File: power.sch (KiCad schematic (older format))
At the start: 32 parts, among them J2 4DB-P108-06, J3 39531-1002, J4 39531-1002, U2 AP1501A-50K5G-13, U3 AP2112K-3.3TRG1

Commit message: Current snapshot
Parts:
- added FB1: MPZ1608S221A, Resistor_SMD:R_0603_1608Metric, symbol Device:Ferrite_Bead_Small
- added JP2: Jumper_3_Bridged12, Connector_PinHeader_2.54mm:PinHeader_1x03_P2.54mm_Vertical, symbol Jumper:Jumper_3_Bridged12
- C1, C3, C4, C5, C6: footprint Capacitor_SMD:CP_Elec_6.3x7.7 -> Capacitor_SMD:CP_Elec_6.3x5.7
- C14: value 10uF -> 22uF; footprint Capacitor_SMD:C_0603_1608Metric -> Capacitor_SMD:C_1206_3216Metric
- C15: footprint Capacitor_SMD:C_0603_1608Metric -> Capacitor_SMD:C_1206_3216Metric
- J2: Note (none) -> Alternative: OSTYK42106030
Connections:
- net VDD24V: now also JP2.3 (B)
- net VDD5V: now also FB1.2, JP2.1 (A); no longer C14.1, U3.1 (IN), U3.3 (EN)
- new net: C14.1, FB1.1, U3.1 (IN), U3.3 (EN)
- new net VDD_FAN: JP2.2 (C)
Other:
- note added: "FAN Voltage Selection"
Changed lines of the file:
@@
 $Descr A4 11693 8268
 encoding utf-8
-Sheet 3 7
+Sheet 3 11
 Title ""
 Date ""
@@
 F 0 "C1" H 1368 1946 50  0000 L CNN
 F 1 "100uF" H 1368 1855 50  0000 L CNN
-F 2 "Capacitor_SMD:CP_Elec_6.3x7.7" H 1288 1750 50  0001 C CNN
-F 3 "https://www.mouser.de/ProductDetail/Wurth-Electronics/865080545012?qs=0KOYDY2FL297tvB6LOdg5A%3d%3d" H 1250 1900 50  0001 C CNN
+F 2 "Capacitor_SMD:CP_Elec_6.3x5.7" H 1288 1750 50  0001 C CNN
+F 3 "" H 1250 1900 50  0001 C CNN
 	1    1250 1900
 	1    0    0    -1
@@
 Wire Wire Line
 	2750 1000 5050 1000
-$Comp
-L Device:C C14
-U 1 1 5BC5B3FE
-P 7000 1900
-F 0 "C14" H 7115 1946 50  0000 L CNN
-F 1 "10uF" H 7115 1855 50  0000 L CNN
-F 2 "Capacitor_SMD:C_0603_1608Metric" H 7038 1750 50  0001 C CNN
-F 3 "~" H 7000 1900 50  0001 C CNN
-	1    7000 1900
-	1    0    0    -1
-$EndComp
-$Comp
-L Device:C C15
-U 1 1 5BC5B47D
-P 8450 1900
-F 0 "C15" H 8565 1946 50  0000 L CNN
-F 1 "10uF" H 8565 1855 50  0000 L CNN
-F 2 "Capacitor_SMD:C_0603_1608Metric" H 8488 1750 50  0001 C CNN
-F 3 "~" H 8450 1900 50  0001 C CNN
-	1    8450 1900
-	1    0    0    -1
-$EndComp
 $Comp
 L Device:R R6
@@
 Wire Wire Line
 	9100 1750 8900 1750
-Connection ~ 8450 1750
-Wire Wire Line
-	8450 1750 8250 1750
 Connection ~ 8900 1750
 Wire Wire Line
-	8900 1750 8450 1750
-Wire Wire Line
-	7000 1750 7350 1750
-Wire Wire Line
 	7350 1750 7350 2050
 Wire Wire Line
 	7350 2050 7550 2050
-Connection ~ 7350 1750
 Wire Wire Line
 	7350 1750 7550 1750
@@
 	1    0    0    -1
 $EndComp
-Text GLabel 6700 1750 0    50   Input ~ 0
+Text GLabel 6350 1750 0    50   Input ~ 0
 VDD5V
-Wire Wire Line
-	6700 1750 7000 1750
-Connection ~ 7000 1750
 Text Notes 1850 800  0    157  ~ 31
 5V Power supply
@@
 F 2 "heteromycin:4DB-P108-06" H 1200 4000 50  0001 C CNN
 F 3 "https://www.mouser.de/datasheet/2/418/NG_CD_2-1437667-4_N8-639207.pdf" H 1200 4000 50  0001 C CNN
+F 4 "Alternative: OSTYK42106030" H 1200 4000 50  0001 C CNN "Note"
 	1    1200 4000
 	-1   0    0    -1
@@
 Text GLabel 4150 3800 2    50   Input ~ 0
 VDD24V
-Text HLabel 4200 4400 2    50   Input ~ 0
-VDD_HEAT1
-Text HLabel 4200 5000 2    50   Input ~ 0
-VDD_HEAT2
 $Comp
 L Device:Fuse F2
@@
 Text Notes 2550 5750 0    50   ~ 0
 15A
-Text HLabel 1400 4200 2    50   Input ~ 0
-VDD_BED
-Text HLabel 1400 4300 2    50   Input ~ 0
-BED_OUT
 $Comp
 L Connector_Generic:Conn_01x02 J3
@@
 	-1   0    0    -1
 $EndComp
-Text HLabel 1400 4700 2    50   Input ~ 0
-VDD_HEAT1
-Text HLabel 1400 4800 2    50   Input ~ 0
-HEAT1_OUT
 $Comp
 L Connector_Generic:Conn_01x02 J4
@@
 	-1   0    0    -1
 $EndComp
-Text HLabel 1400 5200 2    50   Input ~ 0
-VDD_HEAT2
-Text HLabel 1400 5300 2    50   Input ~ 0
-HEAT2_OUT
 Wire Wire Line
 	7000 2350 7900 2350
@@
 	2750 5600 2950 5600
 Connection ~ 2950 5600
-Text HLabel 4200 5600 2    50   Output ~ 0
-VDD_BED
 $Comp
 L Device:Fuse F3
@@
 	2950 5600 3550 5600
 $Comp
+L Device:CP C5
+U 1 1 5BC4FDD0
+P 3550 5150
+F 0 "C5" H 3668 5196 50  0000 L CNN
+F 1 "100uF" H 3668 5105 50  0000 L CNN
+F 2 "Capacitor_SMD:CP_Elec_6.3x5.7" H 3588 5000 50  0001 C CNN
+F 3 "" H 3550 5150 50  0001 C CNN
+	1    3550 5150
+	1    0    0    -1
+$EndComp
+$Comp
+L Device:CP C4
+U 1 1 5BC51306
+P 3550 4550
+F 0 "C4" H 3668 4596 50  0000 L CNN
+F 1 "100uF" H 3668 4505 50  0000 L CNN
+F 2 "Capacitor_SMD:CP_Elec_6.3x5.7" H 3588 4400 50  0001 C CNN
+F 3 "" H 3550 4550 50  0001 C CNN
+	1    3550 4550
+	1    0    0    -1
+$EndComp
+$Comp
 L Device:CP C3
-U 1 1 5BEFFED4
+U 1 1 5BC52840
 P 3550 3950
 F 0 "C3" H 3668 3996 50  0000 L CNN
 F 1 "100uF" H 3668 3905 50  0000 L CNN
-F 2 "Capacitor_SMD:CP_Elec_6.3x7.7" H 3588 3800 50  0001 C CNN
-F 3 "https://www.mouser.de/ProductDetail/Wurth-Electronics/865080545012?qs=0KOYDY2FL297tvB6LOdg5A%3d%3d" H 3550 3950 50  0001 C CNN
+F 2 "Capacitor_SMD:CP_Elec_6.3x5.7" H 3588 3800 50  0001 C CNN
+F 3 "" H 3550 3950 50  0001 C CNN
 	1    3550 3950
 	1    0    0    -1
 $EndComp
 $Comp
-L Device:CP C4
-U 1 1 5BF01408
-P 3550 4550
-F 0 "C4" H 3668 4596 50  0000 L CNN
-F 1 "100uF" H 3668 4505 50  0000 L CNN
-F 2 "Capacitor_SMD:CP_Elec_6.3x7.7" H 3588 4400 50  0001 C CNN
-F 3 "https://www.mouser.de/ProductDetail/Wurth-Electronics/865080545012?qs=0KOYDY2FL297tvB6LOdg5A%3d%3d" H 3550 4550 50  0001 C CNN
-	1    3550 4550
-	1    0    0    -1
-$EndComp
-$Comp
-L Device:CP C5
-U 1 1 5BF0293A
-P 3550 5150
-F 0 "C5" H 3668 5196 50  0000 L CNN
-F 1 "100uF" H 3668 5105 50  0000 L CNN
-F 2 "Capacitor_SMD:CP_Elec_6.3x7.7" H 3588 5000 50  0001 C CNN
-F 3 "https://www.mouser.de/ProductDetail/Wurth-Electronics/865080545012?qs=0KOYDY2FL297tvB6LOdg5A%3d%3d" H 3550 5150 50  0001 C CNN
-	1    3550 5150
-	1    0    0    -1
-$EndComp
-$Comp
 L Device:CP C6
-U 1 1 5BF03E76
+U 1 1 5BC53D94
 P 3550 5750
 F 0 "C6" H 3668 5796 50  0000 L CNN
 F 1 "100uF" H 3668 5705 50  0000 L CNN
-F 2 "Capacitor_SMD:CP_Elec_6.3x7.7" H 3588 5600 50  0001 C CNN
-F 3 "https://www.mouser.de/ProductDetail/Wurth-Electronics/865080545012?qs=0KOYDY2FL297tvB6LOdg5A%3d%3d" H 3550 5750 50  0001 C CNN
+F 2 "Capacitor_SMD:CP_Elec_6.3x5.7" H 3588 5600 50  0001 C CNN
+F 3 "" H 3550 5750 50  0001 C CNN
 	1    3550 5750
 	1    0    0    -1
 $EndComp
+Connection ~ 3550 5600
+Wire Wire Line
+	3550 5600 4050 5600
+Connection ~ 3550 5000
+Wire Wire Line
+	3550 5000 4050 5000
 Connection ~ 3550 4400
 Wire Wire Line
@@
 Wire Wire Line
 	3550 3800 4050 3800
-Connection ~ 3550 5000
-Wire Wire Line
-	3550 5000 4050 5000
-Connection ~ 3550 5600
-Wire Wire Line
-	3550 5600 4050 5600
+$Comp
+L Device:C C14
+U 1 1 5BCBCE1D
+P 7000 1900
+F 0 "C14" H 7115 1946 50  0000 L CNN
+F 1 "22uF" H 7115 1855 50  0000 L CNN
+F 2 "Capacitor_SMD:C_1206_3216Metric" H 7038 1750 50  0001 C CNN
+F 3 "~" H 7000 1900 50  0001 C CNN
+	1    7000 1900
+	1    0    0    -1
+$EndComp
+$Comp
+L Device:Ferrite_Bead_Small FB?
+U 1 1 5BCC4BBE
+P 6650 1750
+AR Path="/5BC1C8A4/5BCC4BBE" Ref="FB?"  Part="1"
+AR Path="/5BC54251/5BCC4BBE" Ref="FB1"  Part="1"
+F 0 "FB1" V 6800 1700 50  0000 C CNN
+F 1 "MPZ1608S221A" V 6900 1700 50  0000 C CNN
+F 2 "Resistor_SMD:R_0603_1608Metric" V 6580 1750 50  0001 C CNN
+F 3 "https://www.mouser.de/datasheet/2/400/eads_commercial_power_mpz1608_en-923650.pdf" H 6650 1750 50  0001 C CNN
+	1    6650 1750
+	0    1    1    0
+$EndComp
+Wire Wire Line
+	6350 1750 6550 1750
+$Comp
+L Device:C C15
+U 1 1 5BCCA55E
+P 8450 1900
+F 0 "C15" H 8565 1946 50  0000 L CNN
+F 1 "10uF" H 8565 1855 50  0000 L CNN
+F 2 "Capacitor_SMD:C_1206_3216Metric" H 8488 1750 50  0001 C CNN
+F 3 "~" H 8450 1900 50  0001 C CNN
+	1    8450 1900
+	1    0    0    -1
+$EndComp
+Wire Wire Line
+	8250 1750 8450 1750
+Connection ~ 8450 1750
+Wire Wire Line
+	8450 1750 8900 1750
+Wire Wire Line
+	6750 1750 7000 1750
+Wire Wire Line
+	7000 1750 7350 1750
+Connection ~ 7000 1750
+Connection ~ 7350 1750
+Text GLabel 4200 5600 2    50   Input ~ 0
+VDD_BED
+Text GLabel 4200 4400 2    50   Input ~ 0
+VDD_HEAT1
+Text GLabel 4200 5000 2    50   Input ~ 0
+VDD_HEAT2
+Text GLabel 1400 4200 2    50   Input ~ 0
+VDD_BED
+Text GLabel 1400 4700 2    50   Input ~ 0
+VDD_HEAT1
+Text GLabel 1400 5200 2    50   Input ~ 0
+VDD_HEAT2
+Text GLabel 1400 4300 2    50   Input ~ 0
+BED_OUT
+Text GLabel 1400 4800 2    50   Input ~ 0
+HEAT1_OUT
+Text GLabel 1400 5300 2    50   Input ~ 0
+HEAT2_OUT
+$Comp
+L Jumper:Jumper_3_Bridged12 JP2
+U 1 1 5BC68888
+P 7900 3850
+F 0 "JP2" H 7900 4054 50  0000 C CNN
+F 1 "Jumper_3_Bridged12" H 7900 3963 50  0000 C CNN
+F 2 "Connector_PinHeader_2.54mm:PinHeader_1x03_P2.54mm_Vertical" H 7900 3850 50  0001 C CNN
+F 3 "~" H 7900 3850 50  0001 C CNN
+	1    7900 3850
+	1    0    0    -1
+$EndComp
+Text GLabel 7650 3850 0    50   Input ~ 0
+VDD5V
+Text GLabel 8150 3850 2    50   Input ~ 0
+VDD24V
+Text GLabel 7900 4000 3    50   Input ~ 0
+VDD_FAN
+Text Notes 6450 3150 0    157  ~ 31
+FAN Voltage Selection
 $EndSCHEMATC

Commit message: Some small adjustments
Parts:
- D5: footprint Diode_SMD:D_SOD-123F -> Diode_SMD:D_SOD-123
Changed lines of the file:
@@
 F 0 "D5" V 3454 1979 50  0000 L CNN
 F 1 "S310FA" V 3545 1979 50  0000 L CNN
-F 2 "Diode_SMD:D_SOD-123F" H 3500 1900 50  0001 C CNN
+F 2 "Diode_SMD:D_SOD-123" H 3500 1900 50  0001 C CNN
 F 3 "https://www.mouser.de/datasheet/2/308/S310FA-1307029.pdf" H 3500 1900 50  0001 C CNN
 	1    3500 1900

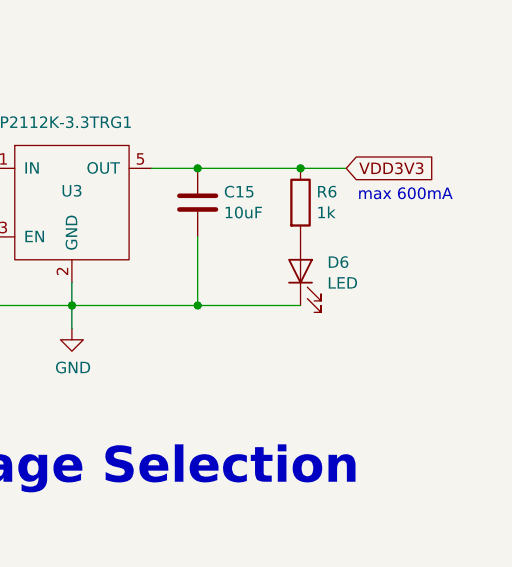
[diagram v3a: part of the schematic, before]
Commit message: Various changes
* Add Status LED
* Switched small diodes to more general available BAT54 in SOD123
* Fixed various DRC errors
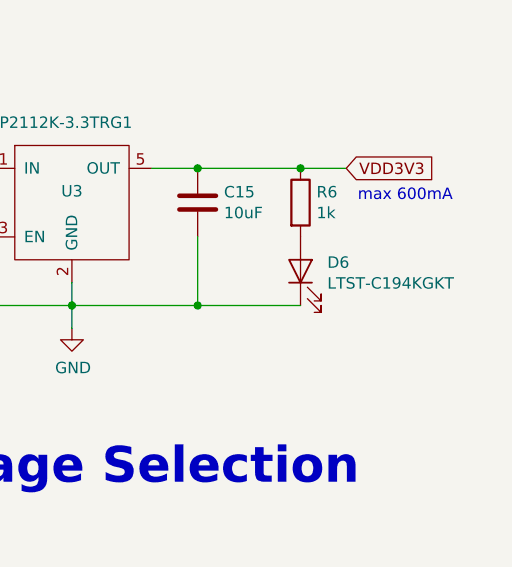
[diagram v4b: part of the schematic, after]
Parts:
- D6: value LED -> LTST-C194KGKT
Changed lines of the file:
@@
 P 8900 2200
 F 0 "D6" V 8938 2083 50  0000 R CNN
-F 1 "LED" V 8847 2083 50  0000 R CNN
+F 1 "LTST-C194KGKT" V 8847 2083 50  0000 R CNN
 F 2 "LED_SMD:LED_0603_1608Metric" H 8900 2200 50  0001 C CNN
 F 3 "~" H 8900 2200 50  0001 C CNN

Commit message: Complete functional design
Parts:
- removed C13: 22uF, Capacitor_SMD:C_1206_3216Metric, symbol Device:C
- removed D5: S310FA, Diode_SMD:D_SOD-123, symbol Device:D_Schottky
- removed L1: 22uH, heteromycin:SRP1038A-220M, symbol Device:L
- removed U2: AP1501A-50K5G-13, Package_TO_SOT_SMD:TO-263-5_TabPin3, symbol heteromycin:AP1501A-50K5G-13
- added R6: 20k, Resistor_SMD:R_0603_1608Metric, symbol Device:R
- added R7: 15k, Resistor_SMD:R_0603_1608Metric, symbol Device:R
- added U2: i3A, heteromycin:i3A, symbol heteromycin:i3A
- C12: value 22uF -> 100nF
- C2: value 10uF -> 100nF; footprint Capacitor_SMD:C_1206_3216Metric -> Capacitor_SMD:C_1812_4532Metric
- renumbered C14 to C13, C15 to C14, D6 to D5, R6 to R8
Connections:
- net GND: now also R6.2, R7.2, U2.2 (ON/OFF), U2.3 (GND), U2.4 (GND)
- net VDD24V: now also U2.1 (VIN)
- net VDD5V: now also U2.7 (SENSE+), U2.8 (VOUT)
- new net: R6.1, R7.1, U2.6 (TRIM)
- no-connect marks 0 -> 1
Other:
- note added: "8.57 kOhm"
- note added: "max 8A"
- note removed: "max 5A"
- moved on the sheet: C1, C11, C12
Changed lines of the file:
@@
 $EndDescr
-$Comp
-L heteromycin:AP1501A-50K5G-13 U2
-U 1 1 5BC55592
-P 2750 1750
-F 0 "U2" H 2700 1750 50  0000 L CNN
-F 1 "AP1501A-50K5G-13" H 1750 2200 50  0000 L CNN
-F 2 "Package_TO_SOT_SMD:TO-263-5_TabPin3" H 2750 1750 50  0001 C CNN
-F 3 "https://www.mouser.de/datasheet/2/115/AP1501A-85813.pdf" H 2750 1750 50  0001 C CNN
-	1    2750 1750
-	1    0    0    -1
-$EndComp
 $Comp
 L heteromycin:AP2112K-3.3TRG1 U3
@@
 $EndComp
 $Comp
-L Device:D_Schottky D5
-U 1 1 5BC55B92
-P 3500 1900
-F 0 "D5" V 3454 1979 50  0000 L CNN
-F 1 "S310FA" V 3545 1979 50  0000 L CNN
-F 2 "Diode_SMD:D_SOD-123" H 3500 1900 50  0001 C CNN
-F 3 "https://www.mouser.de/datasheet/2/308/S310FA-1307029.pdf" H 3500 1900 50  0001 C CNN
-	1    3500 1900
-	0    1    1    0
-$EndComp
-$Comp
-L Device:L L1
-U 1 1 5BC55D50
-P 3950 1750
-F 0 "L1" V 4140 1750 50  0000 C CNN
-F 1 "22uH" V 4049 1750 50  0000 C CNN
-F 2 "heteromycin:SRP1038A-220M" H 3950 1750 50  0001 C CNN
-F 3 "https://www.mouser.de/ProductDetail/Bourns/SRP1038A-220M?qs=sGAEpiMZZMsg%252by3WlYCkU3WuiCT54zcgeuyXFL0i92Y%3d" H 3950 1750 50  0001 C CNN
-	1    3950 1750
-	0    -1   -1   0
-$EndComp
-Wire Wire Line
-	2750 1000 2750 1250
-Wire Wire Line
-	3300 1750 3500 1750
-Wire Wire Line
-	3800 1750 3500 1750
-Connection ~ 3500 1750
-$Comp
 L power:GND #PWR020
 U 1 1 5BC561B5
@@
 Wire Wire Line
 	3250 2450 3250 2350
-Wire Wire Line
-	3250 2350 2950 2350
-Wire Wire Line
-	2950 2350 2950 2250
-Wire Wire Line
-	2550 2350 2950 2350
-Connection ~ 2950 2350
-Wire Wire Line
-	3250 2350 3500 2350
-Wire Wire Line
-	3500 2350 3500 2050
 Connection ~ 3250 2350
-Text GLabel 5550 1750 2    50   Input ~ 0
+Text GLabel 5500 1250 2    50   Input ~ 0
 VDD5V
-Wire Wire Line
-	4100 1750 4250 1750
 $Comp
 L Device:C C11
 U 1 1 5BC5651E
-P 4250 1900
-F 0 "C11" H 4365 1946 50  0000 L CNN
-F 1 "22uF" H 4365 1855 50  0000 L CNN
-F 2 "Capacitor_SMD:C_1206_3216Metric" H 4288 1750 50  0001 C CNN
-F 3 "~" H 4250 1900 50  0001 C CNN
-	1    4250 1900
-	1    0    0    -1
-$EndComp
-Connection ~ 4250 1750
-$Comp
-L Device:C C12
-U 1 1 5BC565B1
-P 4650 1900
-F 0 "C12" H 4765 1946 50  0000 L CNN
-F 1 "22uF" H 4765 1855 50  0000 L CNN
-F 2 "Capacitor_SMD:C_1206_3216Metric" H 4688 1750 50  0001 C CNN
-F 3 "~" H 4650 1900 50  0001 C CNN
-	1    4650 1900
-	1    0    0    -1
-$EndComp
-Connection ~ 4650 1750
-Wire Wire Line
-	4250 1750 4650 1750
-$Comp
-L Device:C C2
-U 1 1 5BC5686A
-P 1750 1900
-F 0 "C2" H 1865 1946 50  0000 L CNN
-F 1 "10uF" H 1865 1855 50  0000 L CNN
-F 2 "Capacitor_SMD:C_1206_3216Metric" H 1788 1750 50  0001 C CNN
-F 3 "~" H 1750 1900 50  0001 C CNN
-	1    1750 1900
+P 4550 1400
+F 0 "C11" H 4665 1446 50  0000 L CNN
+F 1 "22uF" H 4665 1355 50  0000 L CNN
+F 2 "Capacitor_SMD:C_1206_3216Metric" H 4588 1250 50  0001 C CNN
+F 3 "~" H 4550 1400 50  0001 C CNN
+	1    4550 1400
 	1    0    0    -1
 $EndComp
@@
 L Device:CP C1
 U 1 1 5BC5695B
-P 1250 1900
-F 0 "C1" H 1368 1946 50  0000 L CNN
-F 1 "100uF" H 1368 1855 50  0000 L CNN
-F 2 "Capacitor_SMD:CP_Elec_6.3x5.7" H 1288 1750 50  0001 C CNN
-F 3 "" H 1250 1900 50  0001 C CNN
-	1    1250 1900
-	1    0    0    -1
-$EndComp
-Text GLabel 950  1750 0    50   Input ~ 0
+P 1500 1400
+F 0 "C1" H 1618 1446 50  0000 L CNN
+F 1 "100uF" H 1618 1355 50  0000 L CNN
+F 2 "Capacitor_SMD:CP_Elec_6.3x5.7" H 1538 1250 50  0001 C CNN
+F 3 "" H 1500 1400 50  0001 C CNN
+	1    1500 1400
+	1    0    0    -1
+$EndComp
+Text GLabel 1200 1250 0    50   Input ~ 0
 VDD24V
 Wire Wire Line
-	950  1750 1250 1750
-Wire Wire Line
-	1250 1750 1750 1750
-Connection ~ 1250 1750
-Wire Wire Line
-	1750 1750 2200 1750
-Connection ~ 1750 1750
-Wire Wire Line
-	1750 2050 1750 2350
-Wire Wire Line
-	1750 2350 2550 2350
-Connection ~ 2550 2350
-Wire Wire Line
-	2550 2250 2550 2350
-Wire Wire Line
-	1250 2050 1250 2350
-Wire Wire Line
-	1250 2350 1750 2350
-Connection ~ 1750 2350
-Wire Wire Line
-	3500 2350 4250 2350
-Wire Wire Line
-	4250 2350 4250 2050
-Connection ~ 3500 2350
-Wire Wire Line
-	4250 2350 4650 2350
-Wire Wire Line
-	4650 2350 4650 2050
-Connection ~ 4250 2350
-$Comp
-L Device:C C13
-U 1 1 5BC584E1
-P 5050 1900
-F 0 "C13" H 5165 1946 50  0000 L CNN
-F 1 "22uF" H 5165 1855 50  0000 L CNN
-F 2 "Capacitor_SMD:C_1206_3216Metric" H 5088 1750 50  0001 C CNN
-F 3 "~" H 5050 1900 50  0001 C CNN
-	1    5050 1900
-	1    0    0    -1
-$EndComp
-Wire Wire Line
-	4650 1750 5050 1750
-Connection ~ 5050 1750
-Wire Wire Line
-	5050 1750 5550 1750
-Wire Wire Line
-	5050 2050 5050 2350
-Wire Wire Line
-	5050 2350 4650 2350
-Connection ~ 4650 2350
-Wire Wire Line
-	5050 1000 5050 1750
-Wire Wire Line
-	2750 1000 5050 1000
-$Comp
-L Device:R R6
+	1200 1250 1500 1250
+$Comp
+L Device:R R8
 U 1 1 5BC5B537
 P 8900 1900
-F 0 "R6" H 8970 1946 50  0000 L CNN
+F 0 "R8" H 8970 1946 50  0000 L CNN
 F 1 "1k" H 8970 1855 50  0000 L CNN
 F 2 "Resistor_SMD:R_0603_1608Metric" V 8830 1900 50  0001 C CNN
@@
 $EndComp
 $Comp
-L Device:LED D6
+L Device:LED D5
 U 1 1 5BC5B5D6
 P 8900 2200
-F 0 "D6" V 8938 2083 50  0000 R CNN
+F 0 "D5" V 8938 2083 50  0000 R CNN
 F 1 "LTST-C194KGKT" V 8847 2083 50  0000 R CNN
 F 2 "LED_SMD:LED_0603_1608Metric" H 8900 2200 50  0001 C CNN
@@
 Wire Wire Line
 	7000 2050 7000 2350
-Text Notes 5600 1900 0    50   ~ 0
-max 5A
+Text Notes 5550 1400 0    50   ~ 0
+max 8A
 Text Notes 9150 1900 0    50   ~ 0
 max 600mA
@@
 	3550 3800 4050 3800
 $Comp
-L Device:C C14
+L Device:C C13
 U 1 1 5BCBCE1D
 P 7000 1900
-F 0 "C14" H 7115 1946 50  0000 L CNN
+F 0 "C13" H 7115 1946 50  0000 L CNN
 F 1 "22uF" H 7115 1855 50  0000 L CNN
 F 2 "Capacitor_SMD:C_1206_3216Metric" H 7038 1750 50  0001 C CNN
@@
 	6350 1750 6550 1750
 $Comp
-L Device:C C15
+L Device:C C14
 U 1 1 5BCCA55E
 P 8450 1900
-F 0 "C15" H 8565 1946 50  0000 L CNN
+F 0 "C14" H 8565 1946 50  0000 L CNN
 F 1 "10uF" H 8565 1855 50  0000 L CNN
 F 2 "Capacitor_SMD:C_1206_3216Metric" H 8488 1750 50  0001 C CNN
@@
 Text Notes 6450 3150 0    157  ~ 31
 FAN Voltage Selection
+$Comp
+L Device:C C12
+U 1 1 5BC565B1
+P 4950 1400
+F 0 "C12" H 5065 1446 50  0000 L CNN
+F 1 "100nF" H 5065 1355 50  0000 L CNN
+F 2 "Capacitor_SMD:C_1206_3216Metric" H 4988 1250 50  0001 C CNN
+F 3 "~" H 4950 1400 50  0001 C CNN
+	1    4950 1400
+	1    0    0    -1
+$EndComp
+Wire Wire Line
+	3250 2350 3650 2350
+$Comp
+L heteromycin:i3A U2
+U 1 1 5BCDC650
+P 3000 1650
+F 0 "U2" H 3000 2315 50  0000 C CNN
+F 1 "i3A" H 3000 2224 50  0000 C CNN
+F 2 "heteromycin:i3A" H 3000 1650 50  0001 C CNN
+F 3 "https://www.us.tdk-lambda.com/ftp/specs/i3a_full_datasheet.pdf" H 3000 1650 50  0001 C CNN
+	1    3000 1650
+	1    0    0    -1
+$EndComp
+$Comp
+L Device:R R6
+U 1 1 5BCDDC43
+P 3900 2000
+F 0 "R6" H 3970 2046 50  0000 L CNN
+F 1 "20k" H 3970 1955 50  0000 L CNN
+F 2 "Resistor_SMD:R_0603_1608Metric" V 3830 2000 50  0001 C CNN
+F 3 "~" H 3900 2000 50  0001 C CNN
+	1    3900 2000
+	1    0    0    -1
+$EndComp
+$Comp
+L Device:R R7
+U 1 1 5BCDE830
+P 4150 2000
+F 0 "R7" H 4220 2046 50  0000 L CNN
+F 1 "15k" H 4220 1955 50  0000 L CNN
+F 2 "Resistor_SMD:R_0603_1608Metric" V 4080 2000 50  0001 C CNN
+F 3 "~" H 4150 2000 50  0001 C CNN
+	1    4150 2000
+	1    0    0    -1
+$EndComp
+NoConn ~ 3550 1850
+Wire Wire Line
+	3550 2050 3650 2050
+Wire Wire Line
+	3650 2050 3650 2350
+Connection ~ 3650 2350
+Wire Wire Line
+	3650 2350 3900 2350
+Wire Wire Line
+	2450 2050 2350 2050
+Wire Wire Line
+	2350 2050 2350 2350
+Connection ~ 2350 2350
+Wire Wire Line
+	2350 2350 3250 2350
+Wire Wire Line
+	3900 1850 4150 1850
+Wire Wire Line
+	3900 1650 3900 1850
+Connection ~ 3900 1850
+Wire Wire Line
+	3900 2150 3900 2350
+Connection ~ 3900 2350
+Wire Wire Line
+	3900 2350 4550 2350
+Wire Wire Line
+	3900 2150 4150 2150
+Connection ~ 3900 2150
+Text Notes 4050 2250 0    50   ~ 0
+8.57 kOhm
+Wire Wire Line
+	3550 1650 3900 1650
+Wire Wire Line
+	3550 1250 3750 1250
+Connection ~ 4550 1250
+Wire Wire Line
+	4550 1250 4950 1250
+Connection ~ 4950 1250
+Wire Wire Line
+	4950 1250 5500 1250
+Wire Wire Line
+	4550 1550 4550 2350
+Connection ~ 4550 2350
+Wire Wire Line
+	4550 2350 4950 2350
+Wire Wire Line
+	4950 1550 4950 2350
+Wire Wire Line
+	1500 1250 2050 1250
+Connection ~ 1500 1250
+Wire Wire Line
+	1500 1550 1500 2350
+Wire Wire Line
+	1500 2350 2050 2350
+Wire Wire Line
+	2350 2050 2350 1650
+Wire Wire Line
+	2350 1650 2450 1650
+Connection ~ 2350 2050
+$Comp
+L Device:C C2
+U 1 1 5BCFC548
+P 2050 1400
+F 0 "C2" H 2165 1446 50  0000 L CNN
+F 1 "100nF" H 2165 1355 50  0000 L CNN
+F 2 "Capacitor_SMD:C_1812_4532Metric" H 2088 1250 50  0001 C CNN
+F 3 "" H 2050 1400 50  0001 C CNN
+	1    2050 1400
+	1    0    0    -1
+$EndComp
+Wire Wire Line
+	2050 1550 2050 2350
+Connection ~ 2050 2350
+Wire Wire Line
+	2050 2350 2350 2350
+Wire Wire Line
+	3550 1450 3750 1450
+Wire Wire Line
+	3750 1450 3750 1250
+Connection ~ 3750 1250
+Wire Wire Line
+	3750 1250 4550 1250
+Connection ~ 2050 1250
+Wire Wire Line
+	2050 1250 2450 1250
 $EndSCHEMATC
